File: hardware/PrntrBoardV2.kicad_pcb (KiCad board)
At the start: 2 copper layers, 148.7 x 104.3 mm, 248 parts, among them J10 Conn_01x03_Male, J11 Conn_01x03_Male, J12 Conn_01x03_Male, J13 Conn_01x03_Male, J14 Conn_01x03_Male, J15 Conn_01x03_Male, J16 JST XH, J17 KF350, J18 JST XH, J19 JST XH, J20 KF350, J21 JST XH, J3 USB_B_Micro, J4 JST XH, J5 KF129, J6 KF350, J7 Conn_01x03_Male, J8 Conn_01x03_Male, J9 Conn_01x03_Male, U1 74LVC125, U2 STM32F407VETx, U3 24LC64, U4 AMS1117-3.3, U5 DCBuck, U6 74HCT02, Y1 8MHz

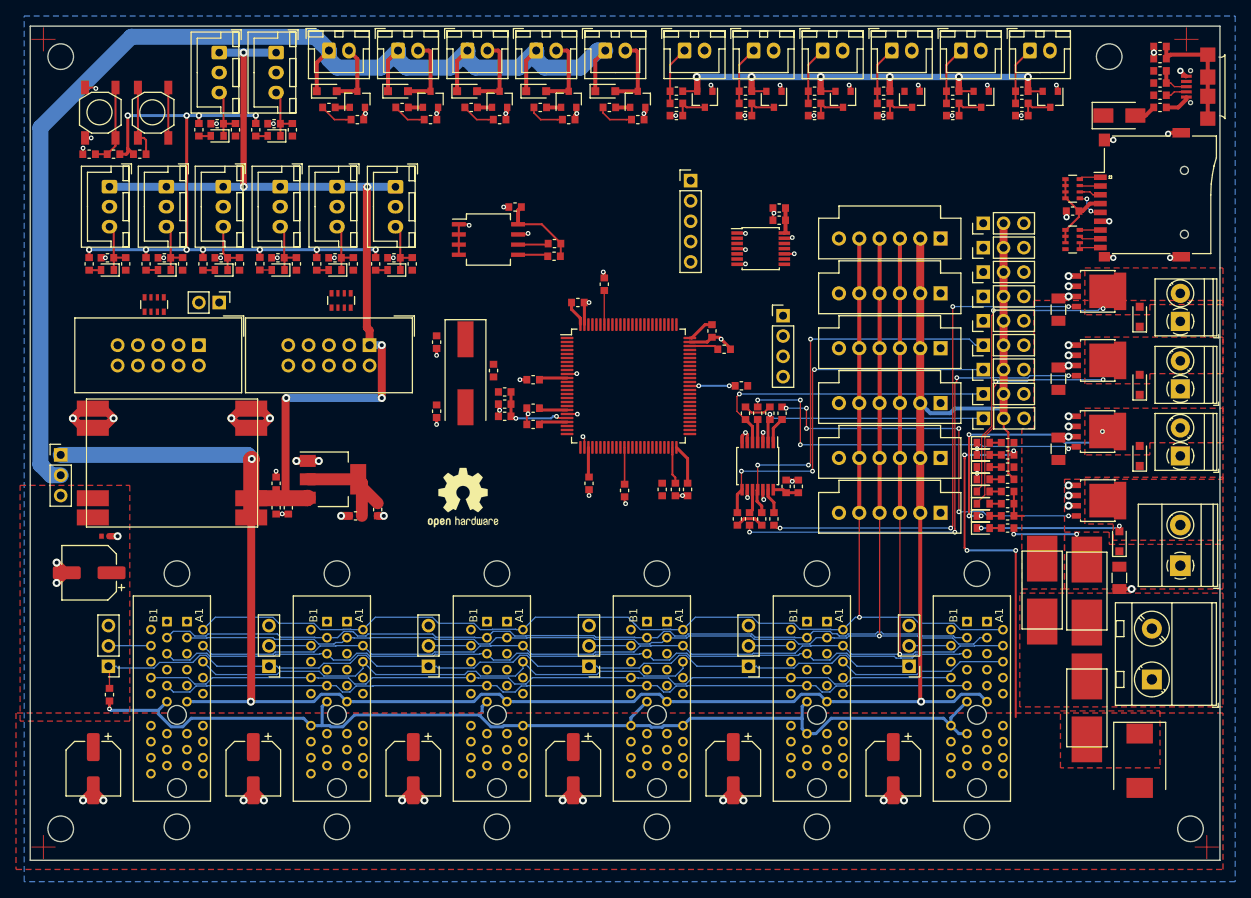
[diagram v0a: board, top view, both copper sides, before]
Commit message: 115 unrouted traces left.
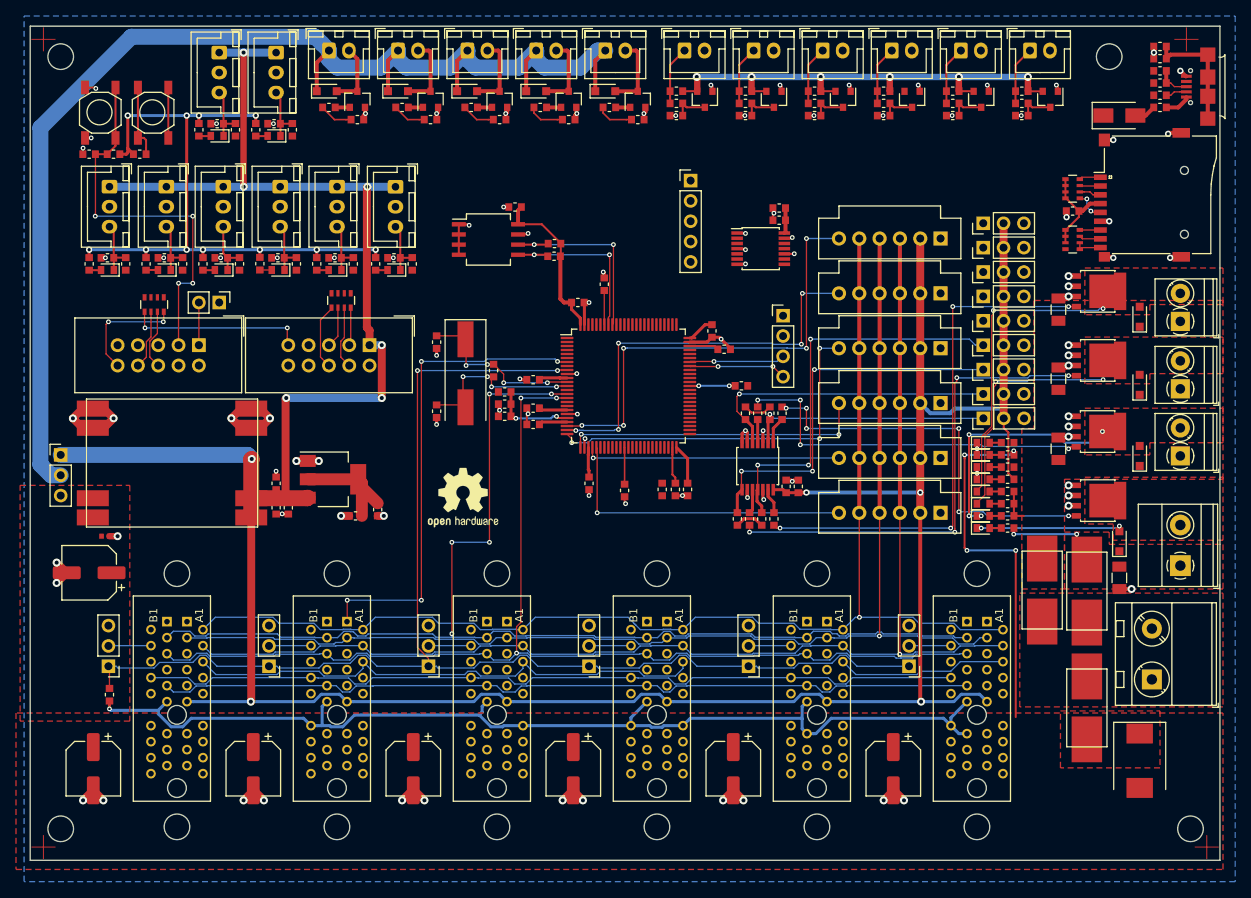
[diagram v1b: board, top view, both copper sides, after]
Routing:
- net ~ST2_CS: track 0.00 -> 60.3 mm, vias 0 -> 4
- net ADC1: track 4.50 -> 61.9 mm, vias 0 -> 5
- net ~ALARM1: track 109.5 -> 165.7 mm, vias 0 -> 2
- net ADC2: track 4.50 -> 55.8 mm, vias 0 -> 5
- net ADC3: track 4.50 -> 50.7 mm, vias 0 -> 3
- net ~ST_ENABLE: track 104.4 -> 149.3 mm, vias 0 -> 5
- net ADC6: track 4.50 -> 42.9 mm, vias 0 -> 1
- net ~ST_RESET: track 105.0 -> 142.9 mm, vias 0 -> 3
- net ADC4: track 4.50 -> 42.4 mm, vias 0 -> 2
- net ~RESET: track 10.2 -> 48.1 mm, vias 0 -> 4
- net ADC5: track 4.50 -> 36.6 mm, vias 0 -> 1
- net Net-(C4-Pad1): track 0.00 -> 22.3 mm, vias 0 -> 4
- net /Sheet5DAF0EF8/E_BTN_ENC: track 0.00 -> 22.0 mm, vias 0 -> 2
- net Net-(C3-Pad1): track 0.00 -> 21.4 mm, vias 0 -> 4
- net I2C_SCL: track 107.1 -> 127.1 mm, vias 0 -> 2
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
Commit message: 100 unrouted traces left.
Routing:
- net V_fan: track 159.0 -> 255.4 mm, vias 0 -> 2
- net ADC6: track 42.9 -> 117.7 mm, vias 1 -> 4
- net /Sheet5DABBBAA/BOOT0: track 10.6 -> 84.1 mm, vias 0 -> 4
- net ADC5: track 36.6 -> 96.9 mm, vias 1 -> 4
- net PWM5: track 4.21 -> 56.6 mm, vias 0 -> 3
- net ADC4: track 42.4 -> 83.7 mm, vias 2 -> 4
- net 3.3V: track 296.8 -> 331.8 mm, vias 12 -> 14
- net PWM4: track 50.3 -> 84.5 mm, vias 3 -> 5
- net ADC3: track 50.7 -> 79.9 mm
- net ADC1: track 61.9 -> 91.0 mm, vias 5 -> 7
- net ADC2: track 55.8 -> 84.3 mm, vias 5 -> 6
- net 5V: track 400.2 -> 426.6 mm, vias 11 -> 13
- net /Sheet5DABBBAA/SWDIO: track 0.00 -> 18.3 mm, vias 0 -> 2
- net /Sheet5DABBBAA/SWDCLK: track 0.00 -> 8.58 mm

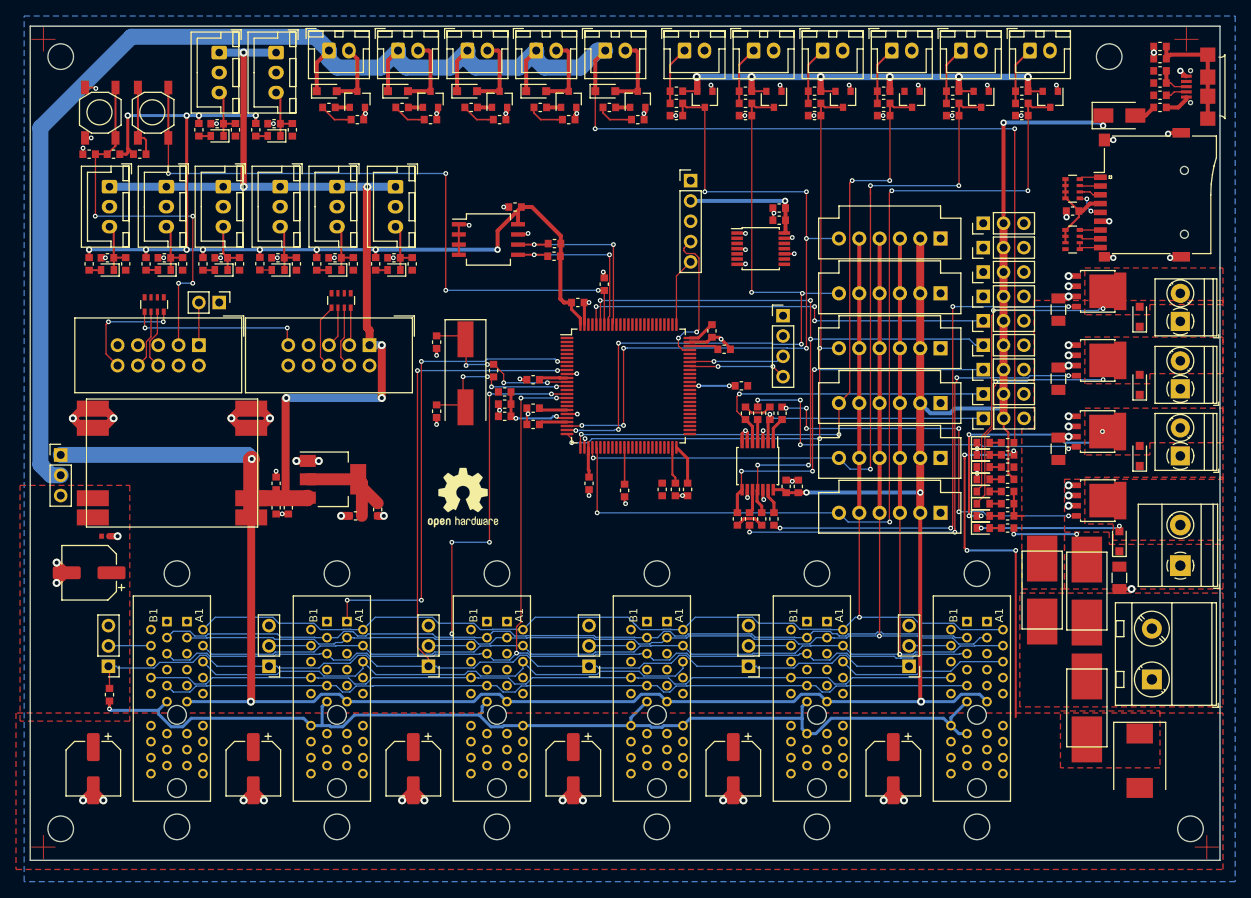
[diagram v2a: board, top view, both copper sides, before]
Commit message: 85 unrouted traces left.
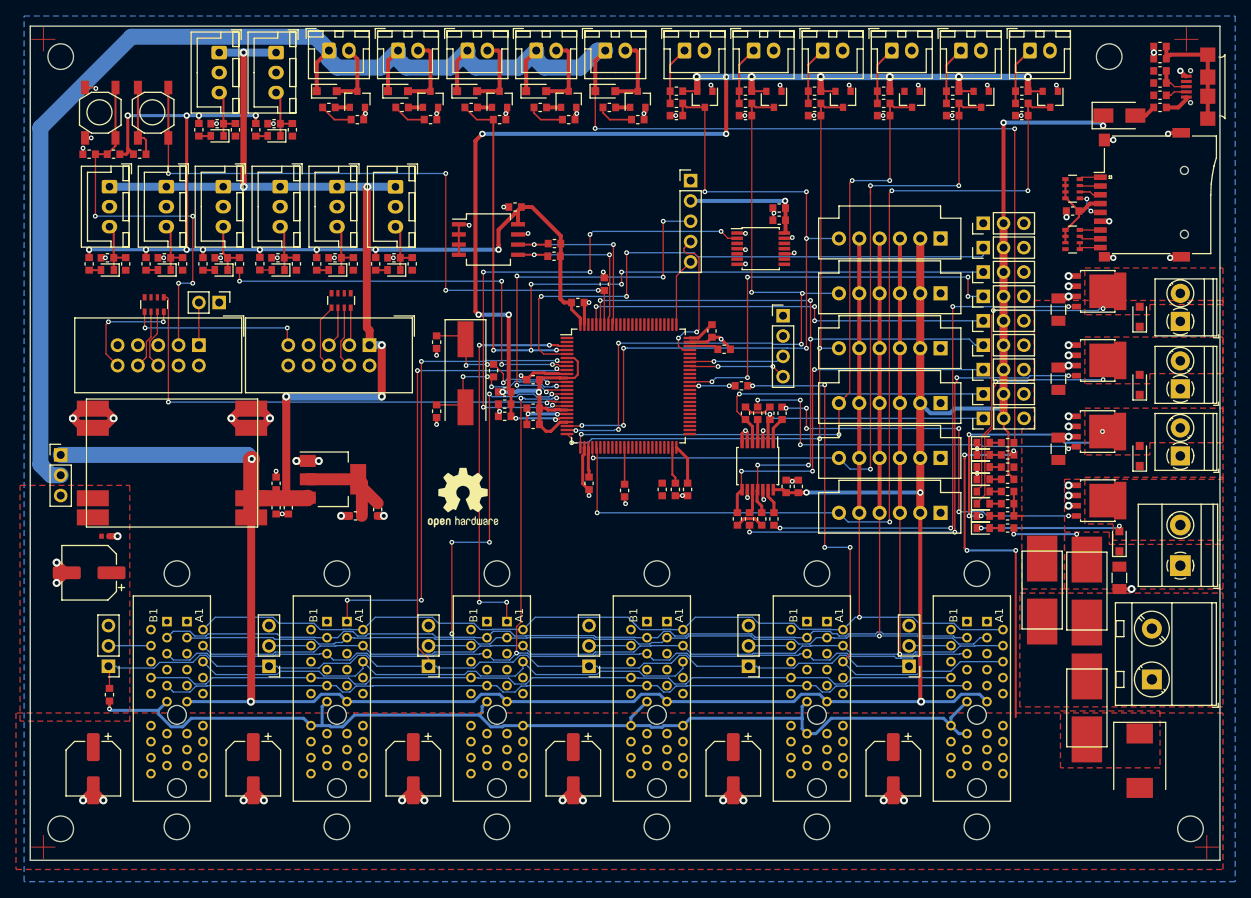
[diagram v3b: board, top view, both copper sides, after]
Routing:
- net PWM7: track 4.21 -> 108.5 mm, vias 0 -> 6
- net AVREF: track 71.6 -> 145.9 mm, vias 8 -> 13
- net PWM8: track 4.58 -> 77.0 mm, vias 0 -> 3
- net /Sheet5DABBBAA/SPI2_MOSI_CPU: track 0.00 -> 64.5 mm, vias 0 -> 6
- net SPI2_MISO: track 0.00 -> 63.6 mm, vias 0 -> 2
- net ~Y_MAX: track 0.00 -> 52.8 mm, vias 0 -> 4
- net PWM6: track 4.21 -> 56.1 mm, vias 0 -> 5
- net ~RESET: track 48.1 -> 97.2 mm, vias 4 -> 9
- net ~ST3_CS: track 0.00 -> 49.0 mm, vias 0 -> 4
- net ST_UART2: track 21.3 -> 69.2 mm, vias 0 -> 4
- net 3.3V: track 331.8 -> 348.2 mm, vias 14 -> 16
- net GND: track 159.8 -> 172.2 mm, vias 104 -> 102
- net Net-(C4-Pad1): track 22.3 -> 22.9 mm
- net ~ST_ENABLE: track 149.3 -> 149.8 mm

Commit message: 89 unrouted traces left.
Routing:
- net USB_D-: track 0.00 -> 90.5 mm, vias 0 -> 4
- net USB_D+: track 0.00 -> 90.3 mm, vias 0 -> 4
- net PWM9: track 4.58 -> 62.6 mm, vias 0 -> 3
- net 3.3V: track 348.2 -> 368.4 mm
- net PWM1: track 30.5 -> 46.7 mm, vias 1 -> 3

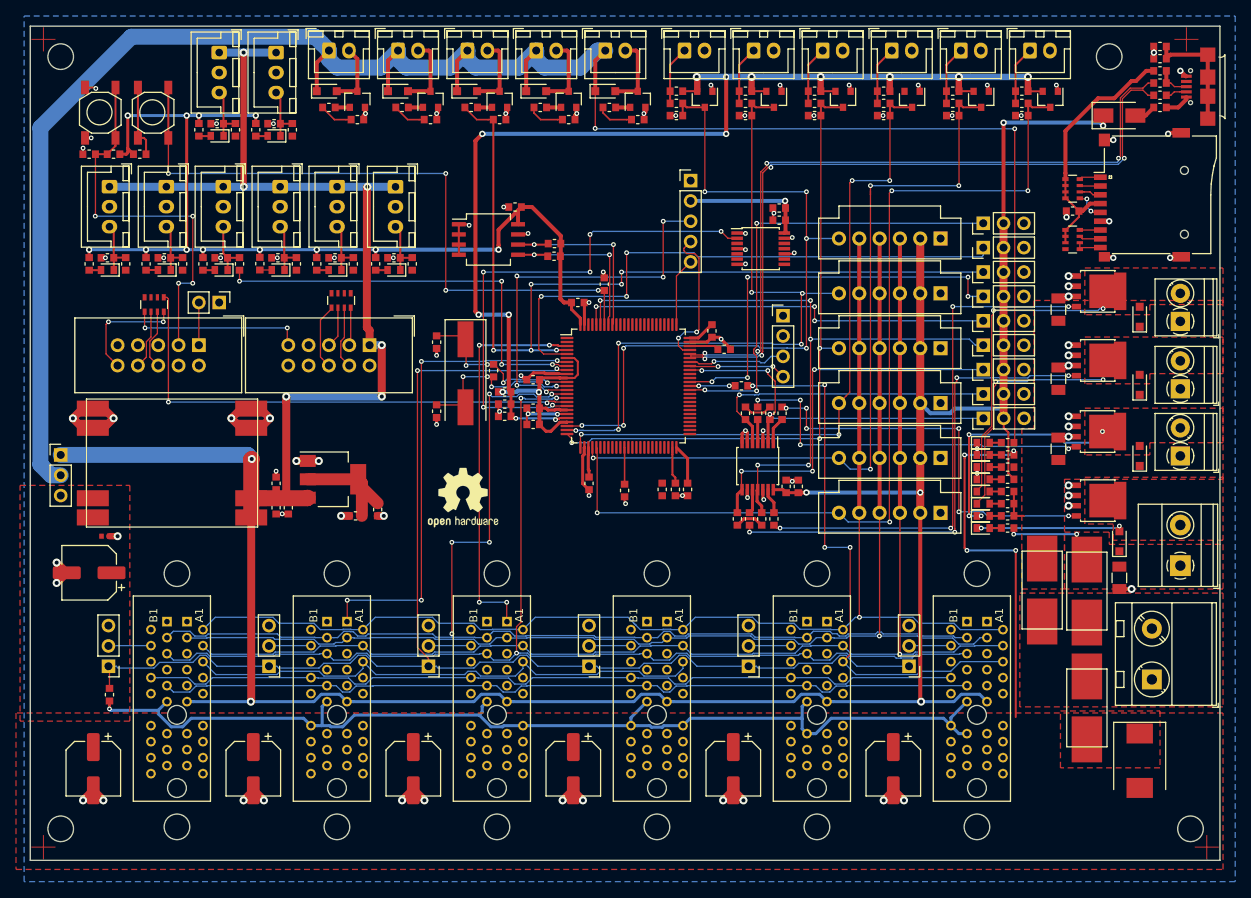
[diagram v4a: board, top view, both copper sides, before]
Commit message: 65 tracks to go. Fixed DRC issues.
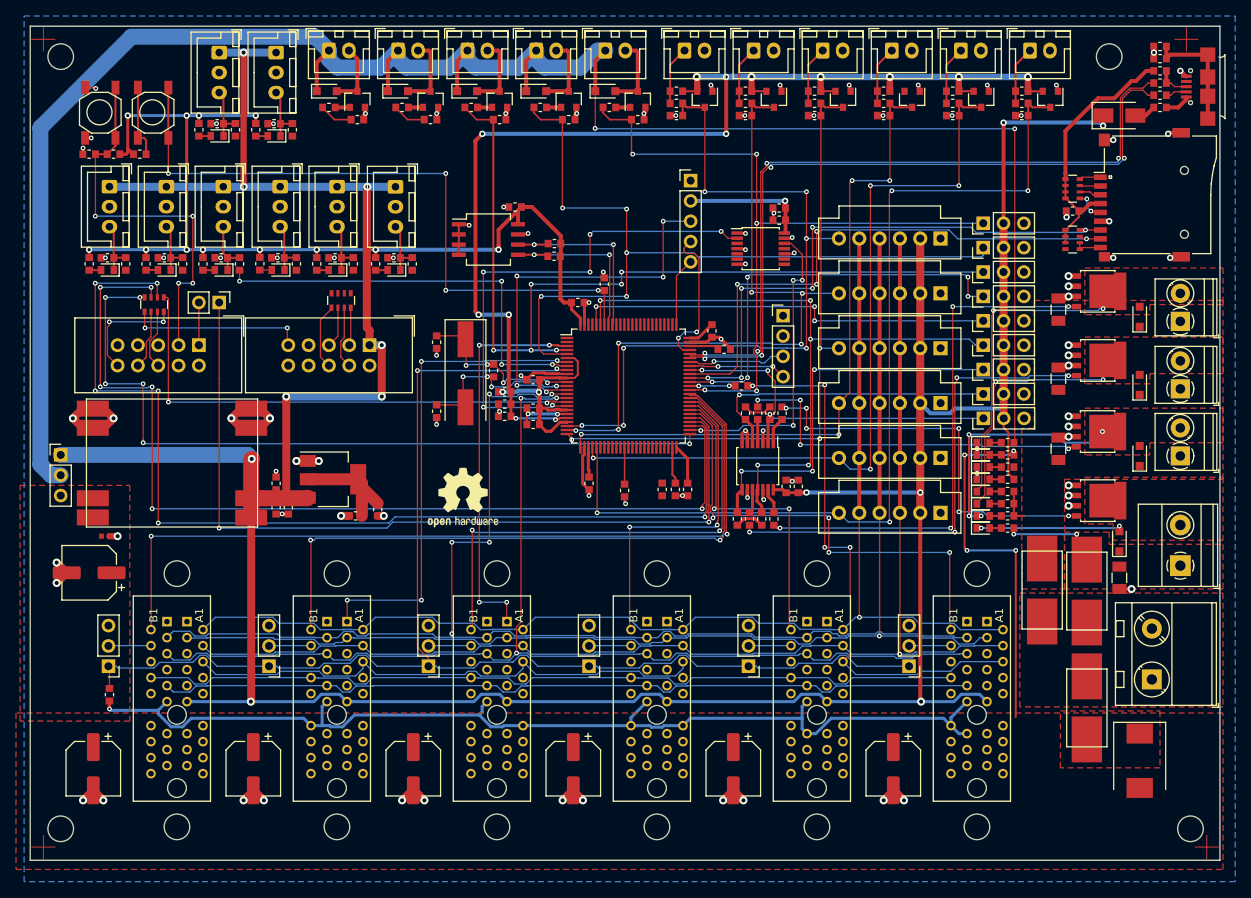
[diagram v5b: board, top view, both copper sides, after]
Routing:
- net ENC_A: track 0.00 -> 129.7 mm, vias 0 -> 6
- net ENC_B: track 0.00 -> 122.8 mm, vias 0 -> 6
- net ~EXP_CS: track 0.00 -> 104.6 mm, vias 0 -> 2
- net ST1_DIR: track 0.00 -> 103.8 mm, vias 0 -> 2
- net BTN_ENC: track 0.00 -> 97.4 mm, vias 0 -> 6
- net ST2_DIR: track 0.00 -> 82.9 mm, vias 0 -> 2
- net SDIO_D0: track 2.57 -> 71.2 mm, vias 0 -> 6
- net SDIO_D1: track 2.70 -> 70.1 mm, vias 0 -> 4
- net ST3_DIR: track 0.00 -> 62.2 mm, vias 0 -> 2
- net ST6_DIR: track 0.00 -> 59.1 mm, vias 0 -> 4
- net ST4_DIR: track 0.00 -> 41.0 mm, vias 0 -> 2
- net ST5_DIR: track 0.00 -> 39.1 mm, vias 0 -> 2
- net /Sheet5DABBBAA/SPI2_SCK_CPU: track 0.00 -> 38.5 mm, vias 0 -> 4
- net PWM9: track 62.6 -> 91.1 mm, vias 3 -> 5
- net PWM8: track 77.0 -> 101.6 mm, vias 3 -> 5
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
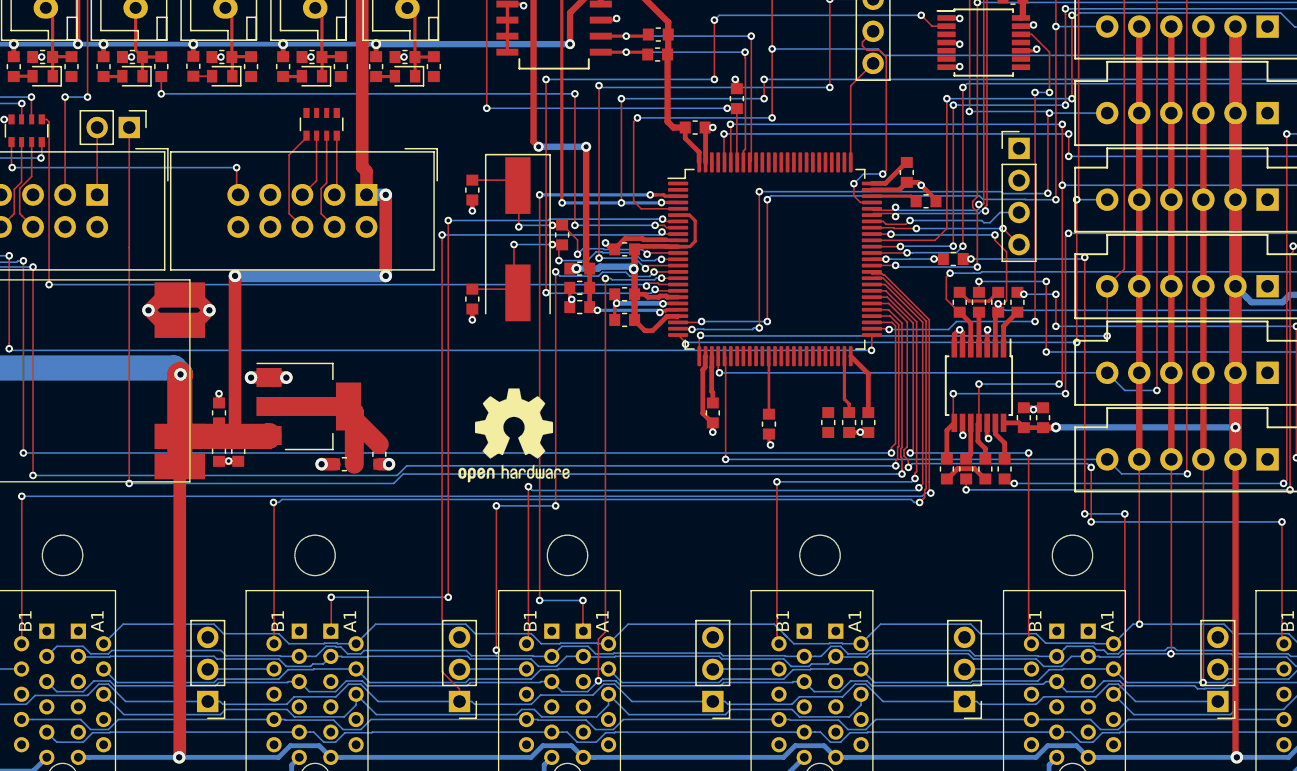
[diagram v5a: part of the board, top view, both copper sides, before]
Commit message: 50 unrouted traces to go.
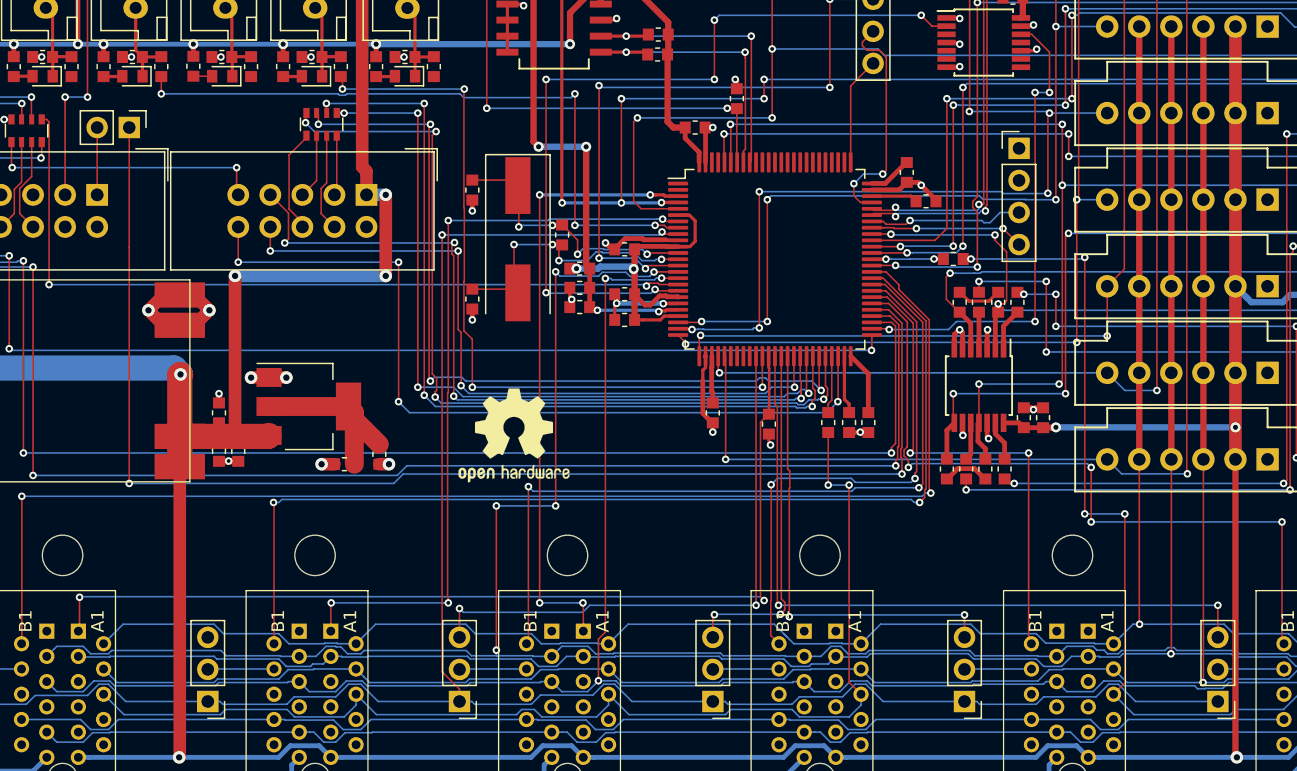
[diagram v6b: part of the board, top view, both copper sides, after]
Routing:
- net ~ST1_CS: track 4.60 -> 76.9 mm, vias 0 -> 2
- net LCD_D4: track 0.00 -> 67.6 mm, vias 0 -> 4
- net LCD_D6: track 0.00 -> 67.0 mm, vias 0 -> 4
- net BEEP: track 0.00 -> 65.7 mm, vias 0 -> 4
- net LCD_D5: track 0.00 -> 64.8 mm, vias 0 -> 4
- net LCD_D7: track 0.00 -> 62.8 mm, vias 0 -> 4
- net LCD_RS: track 0.00 -> 61.4 mm, vias 0 -> 4
- net ~X_MAX: track 0.00 -> 60.1 mm, vias 0 -> 4
- net ~Z_MAX: track 0.00 -> 57.2 mm, vias 0 -> 2
- net ~LCD_E: track 0.00 -> 56.9 mm, vias 0 -> 4
- net ~Z_MIN: track 0.00 -> 45.9 mm, vias 0 -> 2
- net ~V_MIN: track 0.00 -> 36.4 mm, vias 0 -> 2
- net ~U_MIN: track 0.00 -> 27.8 mm, vias 0 -> 2
- net ST_UART1: track 67.0 -> 89.8 mm, vias 0 -> 2
- net /Sheet5DABBBAA/ST_RXTX_1: track 0.00 -> 4.59 mm
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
